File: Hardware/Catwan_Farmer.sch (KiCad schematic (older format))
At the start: 49 parts, among them J1 SENSOR 1, J10 VSP, J2 SENSOR 2, J3 SENSOR 3, J4 BATT, J5 USB_B, J6 Conn_01x04, J7 DHT22, J9 SENSOR 4, SW1 SW_Push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

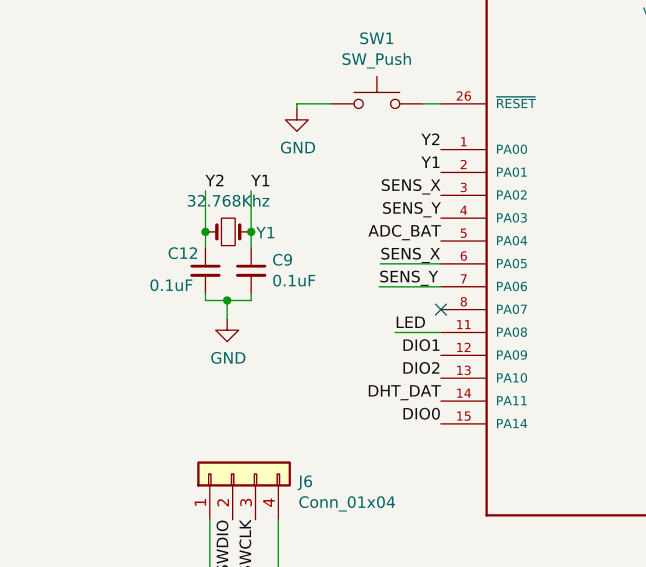
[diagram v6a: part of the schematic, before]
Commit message: add footprint crystal and value c8 and c3, fix footprint u3, u2 usb
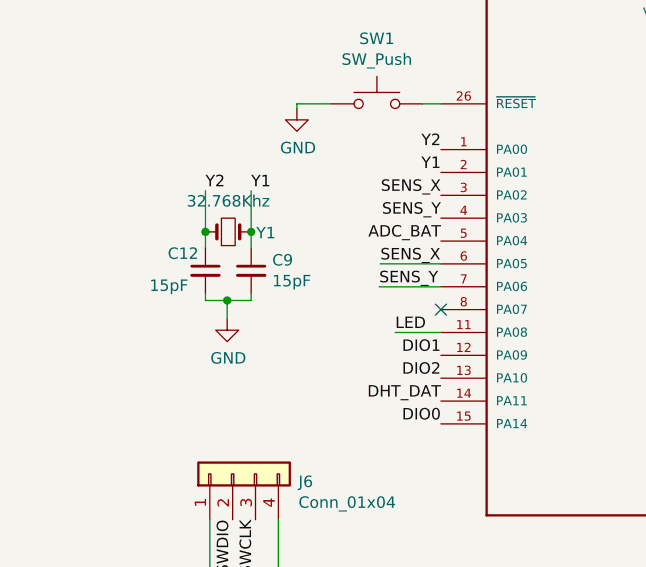
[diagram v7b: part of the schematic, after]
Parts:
- C12, C9: value 0.1uF -> 15pF
- D8: footprint (none) -> Package_TO_SOT_SMD:SOT-23
- J5: footprint Connector_USB:USB_Micro-B_Wuerth_629105150521 -> Connectors electroniccats:U254051N4BH806
- U3: footprint QFN50P500X500X100-33N -> Package_QFP:TQFP-32_7x7mm_P0.8mm; Campo4 ATSAMD21E18A-MU-ND -> (none); Campo5 https://www.digikey.com.mx/product-detail/en/microchip-tech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 -> (none); Campo6 Microchip -> (none); Campo7 ATSAMD21E18A-MU -> (none); Campo8 QFN-32 Microchip -> (none)
- U5: footprint (none) -> Package_SO:SOIC-16_3.9x9.9mm_P1.27mm
- Y1: footprint Crystals:Crystal_AT310_d3.0mm_l10.0mm_Vertical -> Crystal:Crystal_SMD_MicroCrystal_CC7V-T1A-2Pin_3.2x1.5mm_HandSoldering
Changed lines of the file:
@@
 F 0 "J5" H 5364 1971 50  0000 C CNN
 F 1 "USB_B" H 5364 1880 50  0000 C CNN
-F 2 "Connector_USB:USB_Micro-B_Wuerth_629105150521" H 5459 1454 50  0001 C CNN
+F 2 "Connectors electroniccats:U254051N4BH806" H 5459 1454 50  0001 C CNN
 F 3 " ~" H 5459 1454 50  0001 C CNN
 	1    5309 1504
@@
 F 0 "Y1" H 1035 2015 50  0000 C CNN
 F 1 "32.768Khz" H 870 2154 50  0000 C CNN
-F 2 "Crystals:Crystal_AT310_d3.0mm_l10.0mm_Vertical" H 870 2020 50  0001 C CNN
+F 2 "Crystal:Crystal_SMD_MicroCrystal_CC7V-T1A-2Pin_3.2x1.5mm_HandSoldering" H 870 2020 50  0001 C CNN
 F 3 "~" H 870 2020 50  0001 C CNN
 	1    870  2020
@@
 P 770 2190
 F 0 "C12" H 605 2265 50  0000 L CNN
-F 1 "0.1uF" H 525 2125 50  0000 L CNN
+F 1 "15pF" H 525 2125 50  0000 L CNN
 F 2 "Capacitor_SMD:C_0805_2012Metric_Pad1.15x1.40mm_HandSolder" H 770 2190 50  0001 C CNN
 F 3 "~" H 770 2190 50  0001 C CNN
@@
 P 970 2190
 F 0 "C9" H 1062 2236 50  0000 L CNN
-F 1 "0.1uF" H 1062 2145 50  0000 L CNN
+F 1 "15pF" H 1062 2145 50  0000 L CNN
 F 2 "Capacitor_SMD:C_0805_2012Metric_Pad1.15x1.40mm_HandSolder" H 970 2190 50  0001 C CNN
 F 3 "~" H 970 2190 50  0001 C CNN
@@
 F 0 "D8" H 7225 4471 50  0000 C CNN
 F 1 "AZ23C9V1" H 7225 4380 50  0000 C CNN
-F 2 "" H 7225 4255 50  0001 C CNN
+F 2 "Package_TO_SOT_SMD:SOT-23" H 7225 4255 50  0001 C CNN
 F 3 "~" H 7225 4255 50  0001 C CNN
 	1    7225 4255
@@
 F 0 "U3" H 2500 3527 50  0000 C CNN
 F 1 "ATSAMD21E18A-MU" H 2500 3436 50  0000 C CNN
-F 2 "QFN50P500X500X100-33N" H 2500 2160 50  0001 L BNN
+F 2 "Package_QFP:TQFP-32_7x7mm_P0.8mm" H 2500 2160 50  0001 L BNN
 F 3 "SAMD21E Series 256 KB Flash 32 KB SRAM 48 MHz 32-Bit Microcontroller - QFN-32" H 2500 2160 50  0001 L BNN
-F 4 "ATSAMD21E18A-MU-ND" H 2500 2160 50  0001 L BNN "Campo4"
-F 5 "https://www.digikey.com.mx/product-detail/en/microchip-technology/ATSAMD21E18A-MU/ATSAMD21E18A-MU-ND/4935887?utm_source=snapeda&utm_medium=aggregator&utm_campaign=symbol" H 2500 2160 50  0001 L BNN "Campo5"
-F 6 "Microchip" H 2500 2160 50  0001 L BNN "Campo6"
-F 7 "ATSAMD21E18A-MU" H 2500 2160 50  0001 L BNN "Campo7"
-F 8 "QFN-32 Microchip" H 2500 2160 50  0001 L BNN "Campo8"
 	1    2500 2160
 	1    0    0    -1
@@
 F 0 "U5" H 6390 3880 50  0000 C CNN
 F 1 "74HC4052" H 6390 3789 50  0000 C CNN
-F 2 "" H 6390 3310 50  0001 C CNN
+F 2 "Package_SO:SOIC-16_3.9x9.9mm_P1.27mm" H 6390 3310 50  0001 C CNN
 F 3 "Sig/Phil 74hc4052d Smd 50/Tube" H 6390 3310 50  0001 L BNN
 	1    6390 3310

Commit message: End place components
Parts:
- U3: symbol Catwan_Farmer-rescue:ATSAMD21E18A-MU-Electronic_Cats -> Catwan_Farmer-rescue:ATSAMD21E18A-MU-Electronic_Cats-Catwan_Farmer-rescue
- U5: symbol Catwan_Farmer-rescue:74HC4052-Electronic_Cats -> Catwan_Farmer-rescue:74HC4052-Electronic_Cats-Catwan_Farmer-rescue
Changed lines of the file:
@@
 	6975 4725 6965 4725
 $Comp
-L Catwan_Farmer-rescue:ATSAMD21E18A-MU-Electronic_Cats U3
+L Catwan_Farmer-rescue:ATSAMD21E18A-MU-Electronic_Cats-Catwan_Farmer-rescue U3
 U 1 1 5E7C2C42
 P 2500 2160
@@
 $EndComp
 $Comp
-L Catwan_Farmer-rescue:74HC4052-Electronic_Cats U5
+L Catwan_Farmer-rescue:74HC4052-Electronic_Cats-Catwan_Farmer-rescue U5
 U 1 1 5E7C5328
 P 6390 3310
